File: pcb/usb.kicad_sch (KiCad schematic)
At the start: 7 parts, among them J201 USB_C_Receptacle_USB2.0_16P

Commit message: add footprints
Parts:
- D201: footprint (none) -> rp2040-devboard:Texas_X2SON-DPL-2
- D202, D203: footprint (none) -> Diode_SMD:D_SOD-523
- R201, R202: footprint (none) -> Resistor_SMD:R_1210_3225Metric_Pad1.30x2.65mm_HandSolder
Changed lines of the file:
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@@
 			)
 		)
-		(property "Footprint" ""
+		(property "Footprint" "Diode_SMD:D_SOD-523"
 			(at 139.7 130.81 0)
 			(effects
@@
 			)
 		)
-		(property "Footprint" ""
+		(property "Footprint" "rp2040-devboard:Texas_X2SON-DPL-2"
 			(at 146.05 76.2 0)
 			(effects
@@
 			)
 		)
-		(property "Footprint" ""
+		(property "Footprint" "Resistor_SMD:R_1210_3225Metric_Pad1.30x2.65mm_HandSolder"
 			(at 160.782 101.6 90)
 			(effects
@@
 			)
 		)
-		(property "Footprint" ""
+		(property "Footprint" "Resistor_SMD:R_1210_3225Metric_Pad1.30x2.65mm_HandSolder"
 			(at 174.752 101.6 90)
 			(effects
@@
 			)
 		)
-		(property "Footprint" ""
+		(property "Footprint" "Diode_SMD:D_SOD-523"
 			(at 147.32 115.57 0)
 			(effects

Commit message: add footprints
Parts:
- J201: footprint (none) -> Connector_USB:USB_C_Receptacle_GCT_USB4105-xx-A_16P_TopMnt_Horizontal; Distributor link (none) -> https://mou.sr/3RzsrVc
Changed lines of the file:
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@@
 			)
 		)
-		(property "Footprint" ""
+		(property "Footprint" "Connector_USB:USB_C_Receptacle_GCT_USB4105-xx-A_16P_TopMnt_Horizontal"
 			(at 123.19 105.41 0)
 			(effects
@@
 			(at 119.38 105.41 0)
 			(effects
+				(font
+					(size 1.27 1.27)
+				)
+				(hide yes)
+			)
+		)
+		(property "Distributor link" "https://mou.sr/3RzsrVc"
+			(at 119.38 105.41 0)
+			(effects

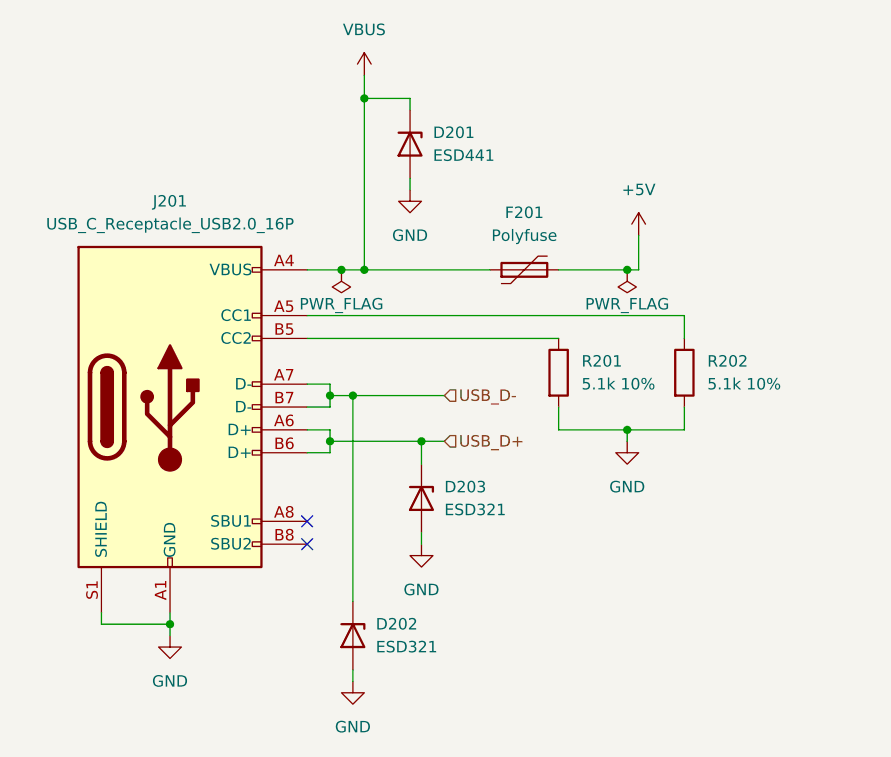
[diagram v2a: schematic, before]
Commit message: add footprints + expose grounds and power on pins
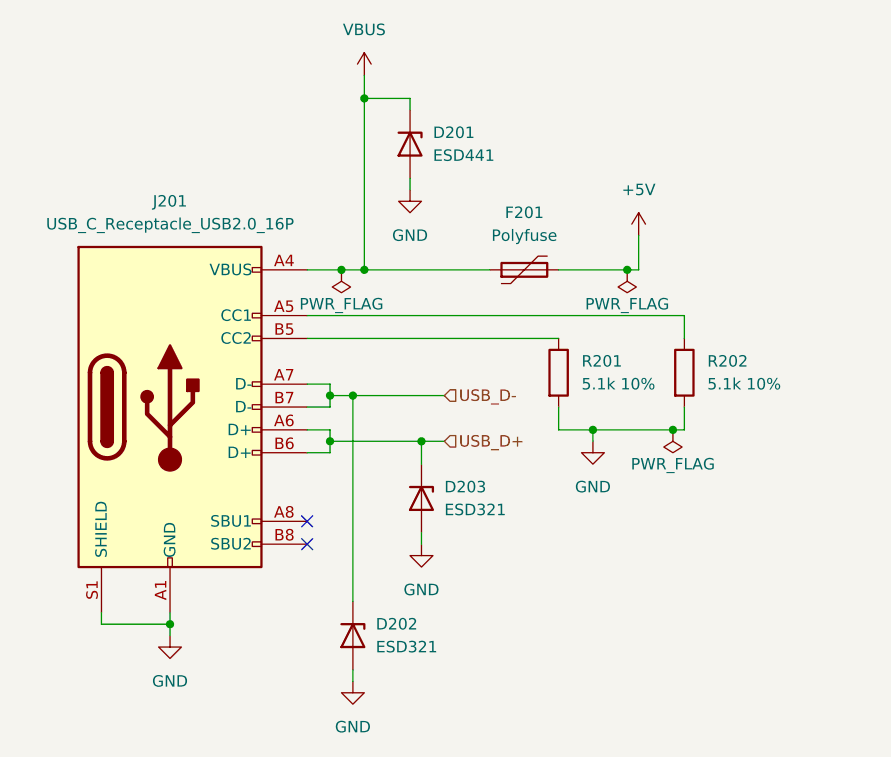
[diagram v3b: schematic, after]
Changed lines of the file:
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@@
 	)
 	(junction
-		(at 170.18 107.95)
+		(at 175.26 107.95)
 		(diameter 0)
 		(color 0 0 0 0)
@@
 	)
 	(junction
+		(at 166.37 107.95)
+		(diameter 0)
+		(color 0 0 0 0)
+	)
+	(junction
 		(at 140.97 71.12)
 		(diameter 0)
@@
 	(wire
 		(pts
-			(xy 170.18 107.95) (xy 176.53 107.95)
-		)
-		(stroke
-			(width 0)
-			(type default)
-		)
-	)
-	(wire
-		(pts
 			(xy 111.76 128.27) (xy 111.76 129.54)
 		)
@@
 	(wire
 		(pts
+			(xy 175.26 107.95) (xy 176.53 107.95)
+		)
+		(stroke
+			(width 0)
+			(type default)
+		)
+	)
+	(wire
+		(pts
 			(xy 162.56 90.17) (xy 170.18 90.17)
 		)
@@
 	(wire
 		(pts
-			(xy 162.56 107.95) (xy 170.18 107.95)
+			(xy 162.56 107.95) (xy 166.37 107.95)
 		)
 		(stroke
@@
 	(wire
 		(pts
-			(xy 170.18 107.95) (xy 170.18 109.22)
+			(xy 166.37 107.95) (xy 166.37 109.22)
+		)
+		(stroke
+			(width 0)
+			(type default)
+		)
+	)
+	(wire
+		(pts
+			(xy 166.37 107.95) (xy 175.26 107.95)
 		)
 		(stroke
@@
 	)
 	(symbol
+		(lib_id "power:PWR_FLAG")
+		(at 175.26 107.95 180)
+		(unit 1)
+		(exclude_from_sim no)
+		(in_bom yes)
+		(on_board yes)
+		(dnp no)
+		(property "Reference" "#FLG03"
+			(at 175.26 109.855 0)
+			(effects
+				(font
+					(size 1.27 1.27)
+				)
+				(hide yes)
+			)
+		)
+		(property "Value" "PWR_FLAG"
+			(at 175.26 111.76 0)
+			(effects
+				(font
+					(size 1.27 1.27)
+				)
+			)
+		)
+		(property "Footprint" ""
+			(at 175.26 107.95 0)
+			(effects
+				(font
+					(size 1.27 1.27)
+				)
+				(hide yes)
+			)
+		)
+		(property "Datasheet" "~"
+			(at 175.26 107.95 0)
+			(effects
+				(font
+					(size 1.27 1.27)
+				)
+				(hide yes)
+			)
+		)
+		(property "Description" "Special symbol for telling ERC where power comes from"
+			(at 175.26 107.95 0)
+			(effects
+				(font
+					(size 1.27 1.27)
+				)
+				(hide yes)
+			)
+		)
+		(pin "1"
+		)
+		(instances
+			(project "rp2040-devboard"
+				(path "/b920ba62-ae29-4be1-8493-2f85fc152395/9891aa85-a7ae-4ee7-907f-2120e5d653bc"
+					(reference "#FLG03")
+					(unit 1)
+				)
+			)
+		)
+	)
+	(symbol
 		(lib_id "power:GND")
-		(at 170.18 109.22 0)
+		(at 166.37 109.22 0)
 		(unit 1)
 		(exclude_from_sim no)
@@
 		(fields_autoplaced yes)
 		(property "Reference" "#PWR020"
-			(at 170.18 115.57 0)
+			(at 166.37 115.57 0)
 			(effects
 				(font
@@
 		)
 		(property "Value" "GND"
-			(at 170.18 114.3 0)
+			(at 166.37 114.3 0)
 			(effects
 				(font
@@
 		)
 		(property "Footprint" ""
-			(at 170.18 109.22 0)
+			(at 166.37 109.22 0)
 			(effects
 				(font
@@
 		)
 		(property "Datasheet" ""
-			(at 170.18 109.22 0)
+			(at 166.37 109.22 0)
 			(effects
 				(font
@@
 		)
 		(property "Description" "Power symbol creates a global label with name \"GND\" , ground"
-			(at 170.18 109.22 0)
-			(effects
-				(font
+			(at 166.37 109.22 0)
+			(effects
+				(font

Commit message: change footprint
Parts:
- R201, R202: footprint Resistor_SMD:R_1210_3225Metric_Pad1.30x2.65mm_HandSolder -> Resistor_SMD:R_0603_1608Metric_Pad0.98x0.95mm_HandSolder
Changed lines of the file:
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@@
 			)
 		)
-		(property "Footprint" "Resistor_SMD:R_1210_3225Metric_Pad1.30x2.65mm_HandSolder"
+		(property "Footprint" "Resistor_SMD:R_0603_1608Metric_Pad0.98x0.95mm_HandSolder"
 			(at 160.782 101.6 90)
 			(effects
@@
 			)
 		)
-		(property "Footprint" "Resistor_SMD:R_1210_3225Metric_Pad1.30x2.65mm_HandSolder"
+		(property "Footprint" "Resistor_SMD:R_0603_1608Metric_Pad0.98x0.95mm_HandSolder"
 			(at 174.752 101.6 90)
 			(effects

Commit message: wip pcb placement
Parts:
- removed D201: ESD441, rp2040-devboard:Texas_X2SON-DPL-2, symbol Device:D_Zener
- removed F201: Polyfuse, symbol Device:Polyfuse
- added C201, C202: 1u, Capacitor_SMD:C_0603_1608Metric_Pad1.08x0.95mm_HandSolder, symbol Device:C
- added U201: NCP360SN, Package_SO:TSOP-5_1.65x3.05mm_P0.95mm, symbol rp2040-devboard:NCP360SN
- renumbered D202 to D201, D203 to D202
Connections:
- net +5V: now also C202.1, U201.5 (OUT)
- net GND: now also C201.2, C202.2, U201.2 (GND), U201.3 (~{EN})
- net VBUS: now also C201.1, U201.1 (IN)
- no-connect marks 2 -> 3
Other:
- moved on the sheet: R201, R202

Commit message: finish routing
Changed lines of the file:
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@@
 	)
 	(hierarchical_label "USB_D+"
-		(shape input)
+		(shape output)
 		(at 149.86 109.22 0)
-		(fields_autoplaced yes)
 		(effects
 			(font
@@
 			(justify left)
 		)
+		(property "Netclass" "USB data"
+			(at 148.844 111.506 0)
+			(effects
+				(font
+					(size 1.27 1.27)
+					(italic yes)
+				)
+				(justify left)
+				(hide yes)
+			)
+		)
 	)
 	(hierarchical_label "USB_D-"
-		(shape input)
+		(shape output)
 		(at 149.86 104.14 0)
-		(fields_autoplaced yes)
 		(effects
 			(font
@@
 			(justify left)
 		)
+		(property "Netclass" "USB data"
+			(at 148.336 106.426 0)
+			(effects
+				(font
+					(size 1.27 1.27)
+					(italic yes)
+				)
+				(justify left)
+				(hide yes)
+			)
+		)
 	)
